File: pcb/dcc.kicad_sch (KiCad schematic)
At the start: 68 parts, among them U10 LM339, U11 LM339, U4 L78L05_SOT89, U5 L79L05_SOT89, U6 LM339, U7 LM339, U8 LM339, U9 4052

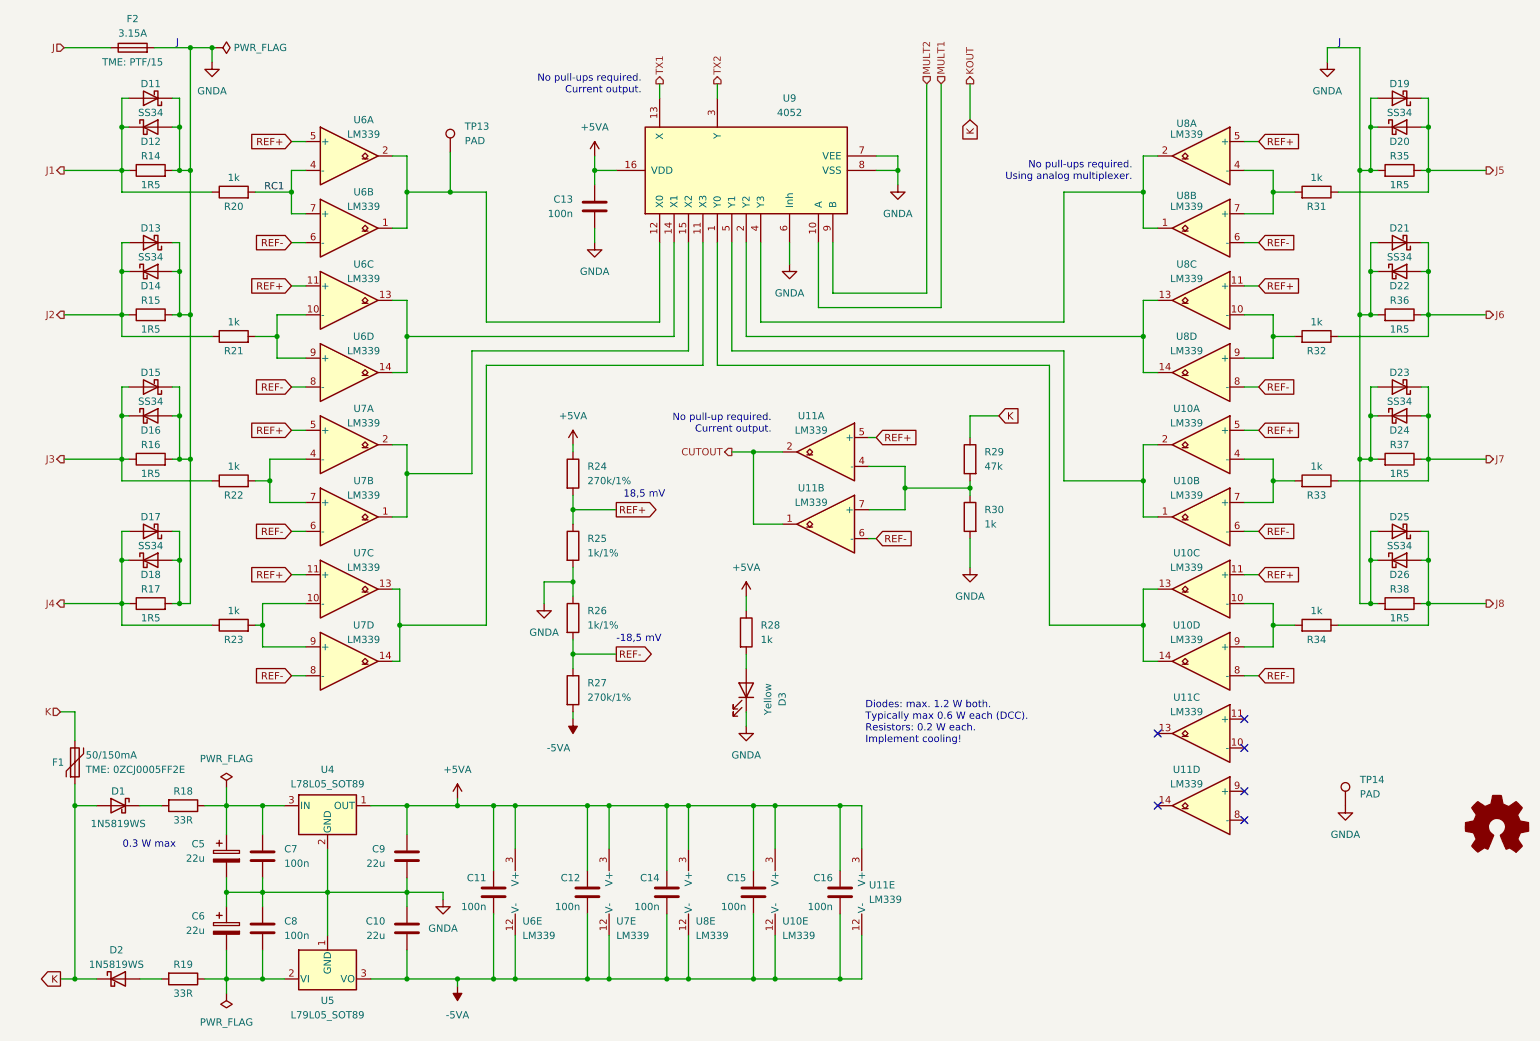
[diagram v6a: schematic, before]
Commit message: pcb: wire dcc voltage stabilization.
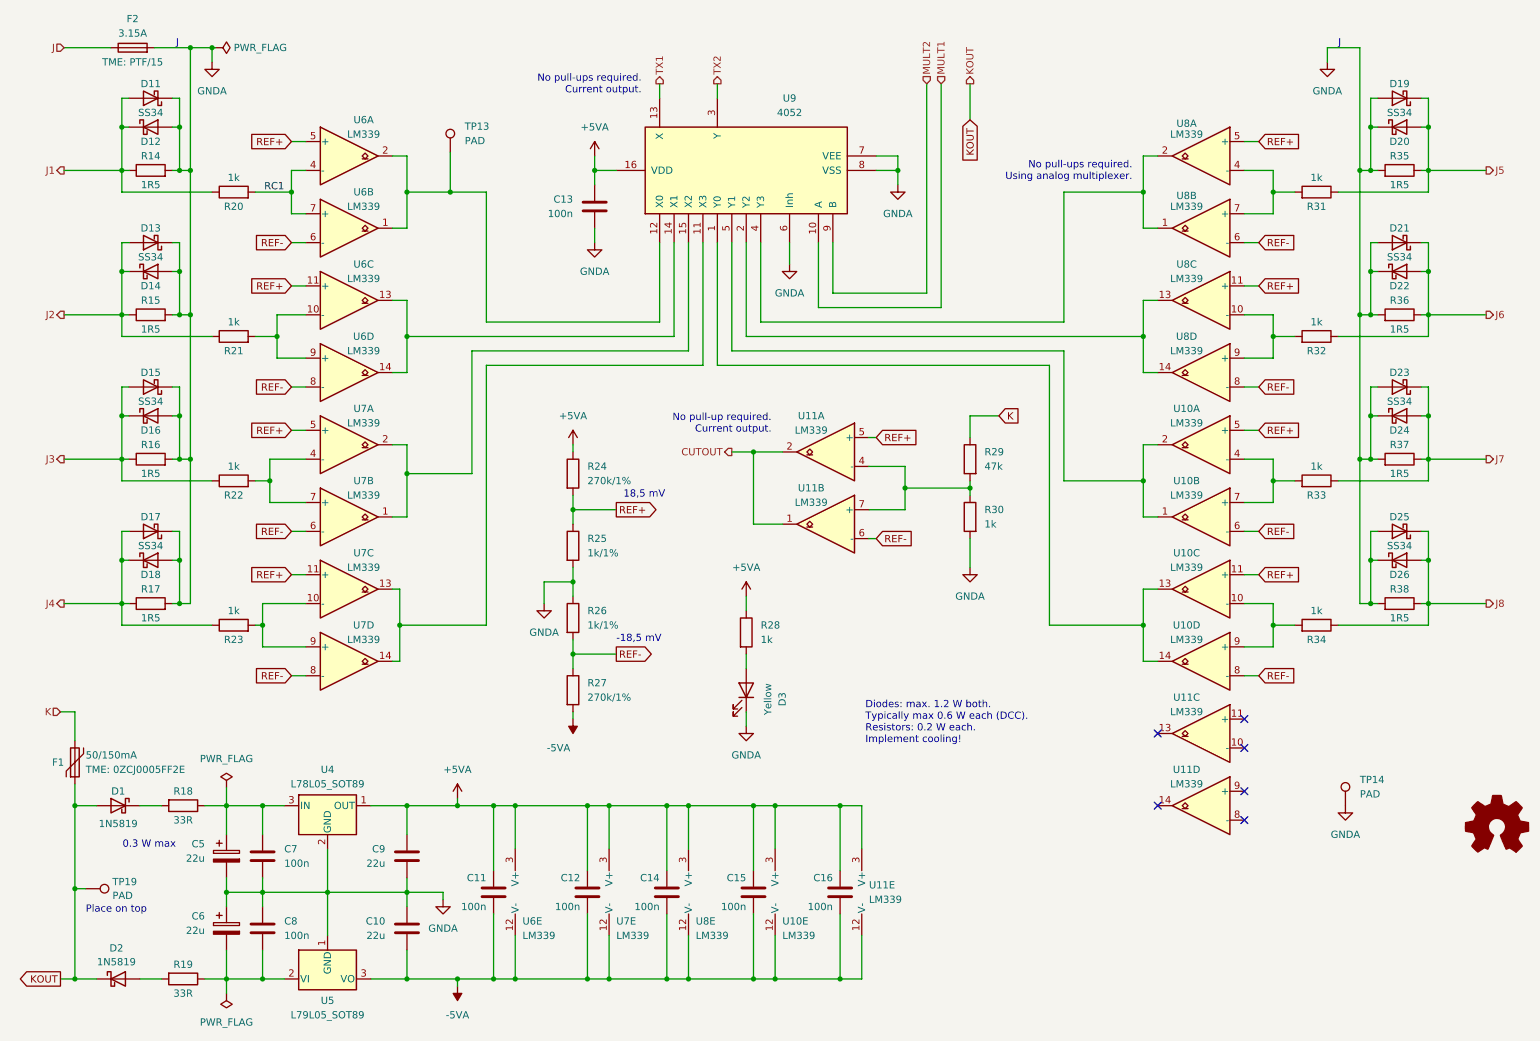
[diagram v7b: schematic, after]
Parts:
- added TP19: PAD, TestPoint:TestPoint_Pad_D2.0mm, symbol Connector:TestPoint
- C10, C11, C12, C14, C15, C16, C7, C8, C9: footprint Capacitor_SMD:C_0805_2012Metric -> Capacitor_SMD:C_0805_2012Metric_Pad1.18x1.45mm_HandSolder
- C5, C6: footprint Capacitor_SMD:C_0805_2012Metric -> Capacitor_Tantalum_SMD:CP_EIA-3216-10_Kemet-I
- D1, D2: value 1N5819WS -> 1N5819
- R24, R25, R26, R27: footprint Resistor_SMD:R_0805_2012Metric -> Resistor_SMD:R_0805_2012Metric_Pad1.20x1.40mm_HandSolder
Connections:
- net K: no longer D1.2 (A), D2.1 (K), F1.1
- new net KOUT: D1.2 (A), D2.1 (K), F1.1, TP19.1
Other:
- note added: "Place on top"
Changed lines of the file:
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@@
   (junction (at 263.525 60.96) (diameter 0) (color 0 0 0 0)
   )
+  (junction (at 25.4 169.545) (diameter 0) (color 0 0 0 0)
+  )
   (junction (at 52.07 170.18) (diameter 0) (color 0 0 0 0)
   )
@@
     (stroke (width 0) (type default))
   )
+  (wire (pts (xy 25.4 169.545) (xy 27.305 169.545))
+    (stroke (width 0) (type default))
+  )
   (wire (pts (xy 129.54 173.99) (xy 129.54 185.42))
     (stroke (width 0) (type default))
@@
     (stroke (width 0) (type default))
   )
-  (wire (pts (xy 25.4 154.94) (xy 25.4 185.42))
+  (wire (pts (xy 25.4 154.94) (xy 25.4 169.545))
     (stroke (width 0) (type default))
   )
@@
     (stroke (width 0) (type default))
   )
+  (wire (pts (xy 25.4 169.545) (xy 25.4 185.42))
+    (stroke (width 0) (type default))
+  )
   (wire (pts (xy 102.87 154.94) (xy 115.57 154.94))
     (stroke (width 0) (type default))
@@
     (effects (font (size 1.27 1.27)) (justify right bottom))
   )
+  (text "Place on top" (at 27.305 173.99 0)
+    (effects (font (size 1.27 1.27)) (justify left bottom))
+  )
   (text "0.3 W max" (at 43.18 162.56 0)
     (effects (font (size 1.27 1.27)) (justify right bottom))
@@
     )
   )
-  (global_label "K" (shape output) (at 22.86 185.42 180) (fields_autoplaced)
+  (global_label "KOUT" (shape output) (at 22.86 185.42 180) (fields_autoplaced)
     (effects (font (size 1.27 1.27)) (justify right))
-    (property "Intersheetrefs" "${INTERSHEET_REFS}" (at 18.6048 185.42 0)
+    (property "Intersheetrefs" "${INTERSHEET_REFS}" (at 14.9762 185.42 0)
       (effects (font (size 1.27 1.27)) (justify right) hide)
     )
@@
     )
   )
-  (global_label "K" (shape input) (at 182.88 34.29 270) (fields_autoplaced)
+  (global_label "KOUT" (shape input) (at 182.88 34.29 270) (fields_autoplaced)
     (effects (font (size 1.27 1.27)) (justify right))
-    (property "Intersheetrefs" "${INTERSHEET_REFS}" (at 182.88 38.5452 90)
+    (property "Intersheetrefs" "${INTERSHEET_REFS}" (at 182.88 42.1738 90)
       (effects (font (size 1.27 1.27)) (justify right) hide)
     )
@@
       (effects (font (size 1.27 1.27)) (justify right))
     )
-    (property "Footprint" "Capacitor_SMD:C_0805_2012Metric" (at 160.9852 173.99 0)
+    (property "Footprint" "Capacitor_SMD:C_0805_2012Metric_Pad1.18x1.45mm_HandSolder" (at 160.9852 173.99 0)
       (effects (font (size 1.27 1.27)) hide)
     )
@@
       (effects (font (size 1.27 1.27)) (justify left))
     )
-    (property "Footprint" "Resistor_SMD:R_0805_2012Metric" (at 111.252 134.62 90)
+    (property "Footprint" "Resistor_SMD:R_0805_2012Metric_Pad1.20x1.40mm_HandSolder" (at 111.252 134.62 90)
       (effects (font (size 1.27 1.27)) hide)
     )
@@
     )
   )
+  (symbol (lib_id "Connector:TestPoint") (at 27.305 169.545 270) (unit 1)
+    (in_bom yes) (on_board yes) (dnp no) (fields_autoplaced)
+    (property "Reference" "TP19" (at 32.004 168.3329 90)
+      (effects (font (size 1.27 1.27)) (justify left))
+    )
+    (property "Value" "PAD" (at 32.004 170.7571 90)
+      (effects (font (size 1.27 1.27)) (justify left))
+    )
+    (property "Footprint" "TestPoint:TestPoint_Pad_D2.0mm" (at 27.305 174.625 0)
+      (effects (font (size 1.27 1.27)) hide)
+    )
+    (property "Datasheet" "~" (at 27.305 174.625 0)
+      (effects (font (size 1.27 1.27)) hide)
+    )
+    (pin "1")
+    (instances
+      (project "railcomdet"
+        (path "/3e59d29f-2657-4552-9290-3c54fadfdf63/e5256faa-a48e-4175-bec4-bd0fa3c5f991"
+          (reference "TP19") (unit 1)
+        )
+      )
+    )
+  )
   (symbol (lib_id "Diode:1N5819WS") (at 33.02 185.42 0) (unit 1)
     (in_bom yes) (on_board yes) (dnp no) (fields_autoplaced)
-    (property "Reference" "D2" (at 32.7025 180.34 0)
+    (property "Reference" "D2" (at 32.7025 180.0057 0)
       (effects (font (size 1.27 1.27)))
     )
-    (property "Value" "1N5819WS" (at 32.7025 182.88 0)
+    (property "Value" "1N5819" (at 32.7025 182.4299 0)
       (effects (font (size 1.27 1.27)))
     )
@@
       (effects (font (size 1.27 1.27)) (justify left))
     )
-    (property "Footprint" "Resistor_SMD:R_0805_2012Metric" (at 111.252 121.92 90)
+    (property "Footprint" "Resistor_SMD:R_0805_2012Metric_Pad1.20x1.40mm_HandSolder" (at 111.252 121.92 90)
       (effects (font (size 1.27 1.27)) hide)
     )
@@
       (effects (font (size 1.27 1.27)) (justify right))
     )
-    (property "Footprint" "Capacitor_SMD:C_0805_2012Metric" (at 53.0352 167.64 0)
+    (property "Footprint" "Capacitor_Tantalum_SMD:CP_EIA-3216-10_Kemet-I" (at 53.0352 167.64 0)
       (effects (font (size 1.27 1.27)) hide)
     )
@@
       (effects (font (size 1.27 1.27)) (justify left))
     )
-    (property "Footprint" "Resistor_SMD:R_0805_2012Metric" (at 111.252 109.22 90)
+    (property "Footprint" "Resistor_SMD:R_0805_2012Metric_Pad1.20x1.40mm_HandSolder" (at 111.252 109.22 90)
       (effects (font (size 1.27 1.27)) hide)
     )
@@
       (effects (font (size 1.27 1.27)) (justify right))
     )
-    (property "Footprint" "Capacitor_SMD:C_0805_2012Metric" (at 145.7452 173.99 0)
+    (property "Footprint" "Capacitor_SMD:C_0805_2012Metric_Pad1.18x1.45mm_HandSolder" (at 145.7452 173.99 0)
       (effects (font (size 1.27 1.27)) hide)
     )
@@
       (effects (font (size 1.27 1.27)) (justify left))
     )
-    (property "Footprint" "Capacitor_SMD:C_0805_2012Metric" (at 59.3852 180.34 0)
+    (property "Footprint" "Capacitor_SMD:C_0805_2012Metric_Pad1.18x1.45mm_HandSolder" (at 59.3852 180.34 0)
       (effects (font (size 1.27 1.27)) hide)
     )
@@
       (effects (font (size 1.27 1.27)) (justify right))
     )
-    (property "Footprint" "Capacitor_SMD:C_0805_2012Metric" (at 130.5052 173.99 0)
+    (property "Footprint" "Capacitor_SMD:C_0805_2012Metric_Pad1.18x1.45mm_HandSolder" (at 130.5052 173.99 0)
       (effects (font (size 1.27 1.27)) hide)
     )
@@
       (effects (font (size 1.27 1.27)) (justify right))
     )
-    (property "Footprint" "Capacitor_SMD:C_0805_2012Metric" (at 53.0352 180.34 0)
+    (property "Footprint" "Capacitor_Tantalum_SMD:CP_EIA-3216-10_Kemet-I" (at 53.0352 180.34 0)
       (effects (font (size 1.27 1.27)) hide)
     )
@@
       (effects (font (size 1.27 1.27)) (justify right))
     )
-    (property "Footprint" "Capacitor_SMD:C_0805_2012Metric" (at 116.5352 173.99 0)
+    (property "Footprint" "Capacitor_SMD:C_0805_2012Metric_Pad1.18x1.45mm_HandSolder" (at 116.5352 173.99 0)
       (effects (font (size 1.27 1.27)) hide)
     )
@@
       (effects (font (size 1.27 1.27)) (justify left))
     )
-    (property "Footprint" "Capacitor_SMD:C_0805_2012Metric" (at 82.8548 180.34 0)
+    (property "Footprint" "Capacitor_SMD:C_0805_2012Metric_Pad1.18x1.45mm_HandSolder" (at 82.8548 180.34 0)
       (effects (font (size 1.27 1.27)) hide)
     )
@@
       (effects (font (size 1.27 1.27)))
     )
-    (property "Value" "1N5819WS" (at 33.02 158.115 0)
+    (property "Value" "1N5819" (at 33.02 158.115 0)
       (effects (font (size 1.27 1.27)))
     )
@@
       (effects (font (size 1.27 1.27)) (justify left))
     )
-    (property "Footprint" "Capacitor_SMD:C_0805_2012Metric" (at 82.8548 167.64 0)
+    (property "Footprint" "Capacitor_SMD:C_0805_2012Metric_Pad1.18x1.45mm_HandSolder" (at 82.8548 167.64 0)
       (effects (font (size 1.27 1.27)) hide)
     )
@@
       (effects (font (size 1.27 1.27)) (justify left))
     )
-    (property "Footprint" "Resistor_SMD:R_0805_2012Metric" (at 111.252 96.52 90)
+    (property "Footprint" "Resistor_SMD:R_0805_2012Metric_Pad1.20x1.40mm_HandSolder" (at 111.252 96.52 90)
       (effects (font (size 1.27 1.27)) hide)
     )
@@
       (effects (font (size 1.27 1.27)) (justify right))
     )
-    (property "Footprint" "Capacitor_SMD:C_0805_2012Metric" (at 100.0252 173.99 0)
+    (property "Footprint" "Capacitor_SMD:C_0805_2012Metric_Pad1.18x1.45mm_HandSolder" (at 100.0252 173.99 0)
       (effects (font (size 1.27 1.27)) hide)
     )
@@
       (effects (font (size 1.27 1.27)) (justify left))
     )
-    (property "Footprint" "Capacitor_SMD:C_0805_2012Metric" (at 59.3852 167.64 0)
+    (property "Footprint" "Capacitor_SMD:C_0805_2012Metric_Pad1.18x1.45mm_HandSolder" (at 59.3852 167.64 0)
       (effects (font (size 1.27 1.27)) hide)
     )
